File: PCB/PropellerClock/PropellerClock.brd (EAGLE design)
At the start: 100 x 50 mm, 32 parts

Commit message: 基板第一弾完成
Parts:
- removed IC2: (no value), v-reg:78XXL
- added C4: (no value), rcl:C2012
- U$2: value CR2032-HOLDER -> CR2032-HOLDER2; device CR2032-holder:CR2032-HOLDER -> CR2032-holder:CR2032-HOLDER2
- moved U$2 12.1 mm to (5.08, 13.3), flipped to the top, turned to 180 degrees
- moved IC1 5.85 mm to (12.1, 38.7)
- moved R1 2.54 mm to (21.0, 40.0)
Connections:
- removed net 3VR: IC1.8, U$2.3VR
- removed net N$1: C2.1, C3.1, IC2.IN, PAD2.1
- new net N$4: IC1.8, U$2.+3V
- net +3V3: now also C2.1, C3.1, C4.1, PAD2.1; no longer IC2.OUT
- net GND: now also C4.2; no longer IC2.GND
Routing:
- net +3V3: track 66.2 -> 91.9 mm
- net N$4: track 0.00 -> 18.4 mm
- net N$1: track 17.2 -> 0.00 mm
- net 3VR: track 15.6 -> 0.00 mm
- net N$8: track 28.7 -> 37.5 mm
- net N$5: track 40.9 -> 48.7 mm
- net GND: track 240.4 -> 235.6 mm
- removed copper zone on layer 16, net 3VR

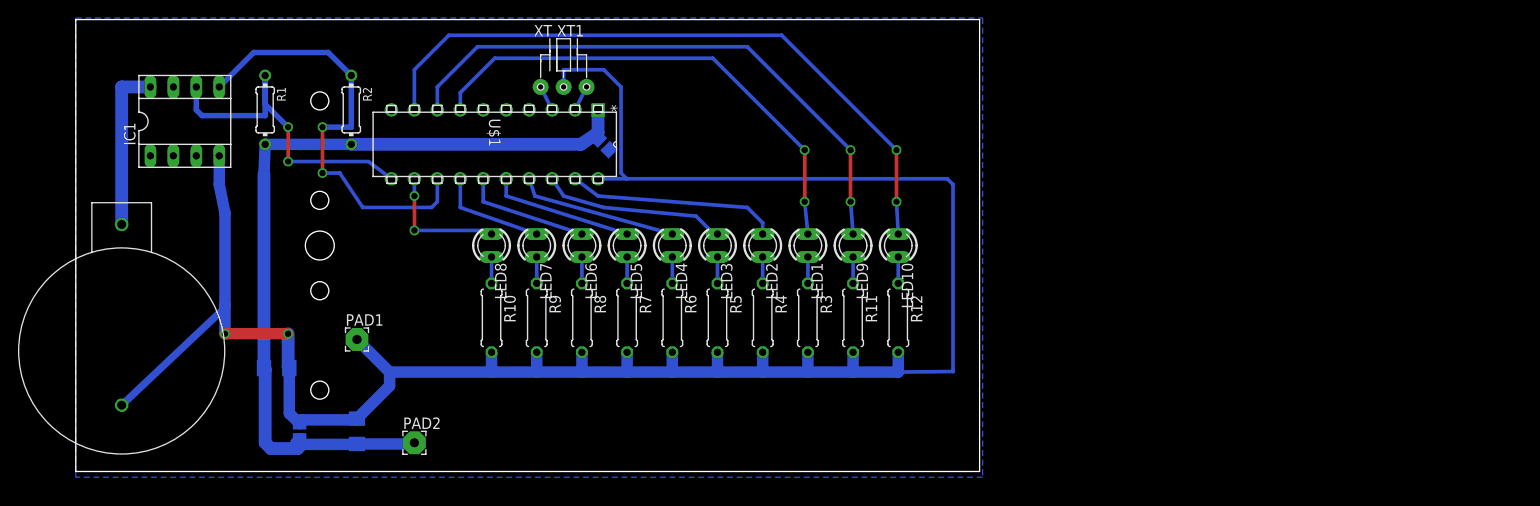
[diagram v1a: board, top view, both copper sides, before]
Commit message: プロペラ部の回路を作成
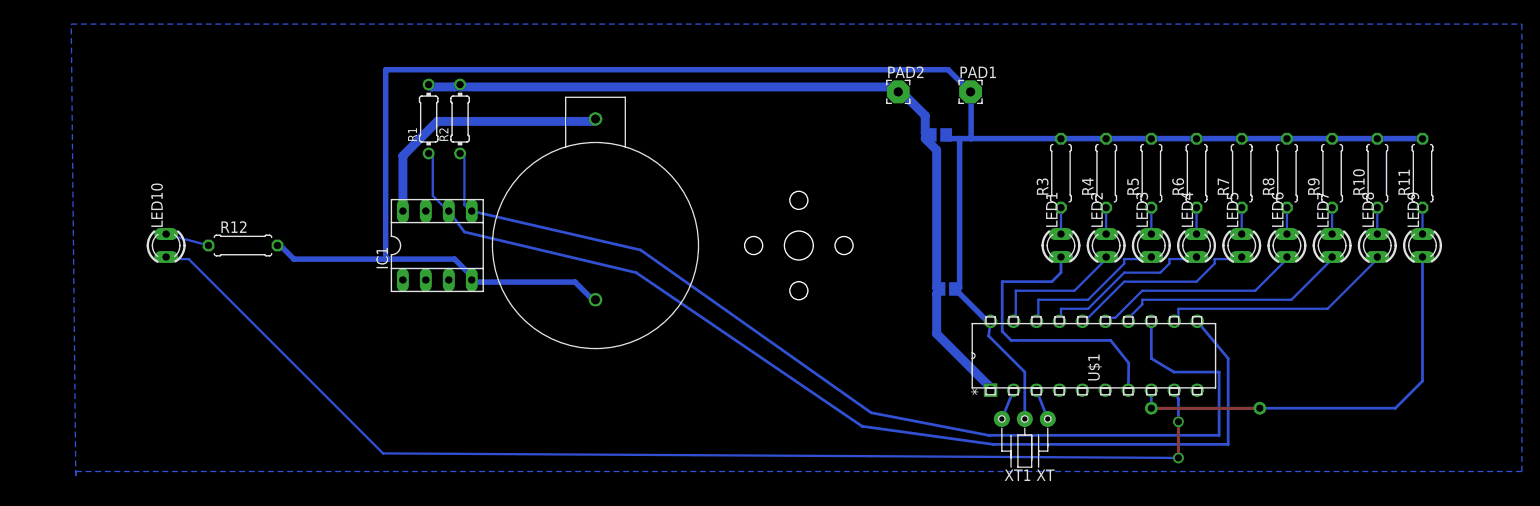
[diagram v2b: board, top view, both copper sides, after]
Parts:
- removed C1, C2: (no value), rcl:C3216
- moved R10 99.3 mm to (144.0, 33.0), turned to 90 degrees
- moved LED8 98.0 mm to (144.0, 25.0), turned to 90 degrees
- moved U$1 90.5 mm to (124.1, 16.6), turned to 90 degrees
- moved R9 89.4 mm to (139.0, 33.0), turned to 90 degrees
- moved LED7 88.0 mm to (139.0, 25.0), turned to 90 degrees
- moved LED10 81.0 mm to (10.0, 25.0), turned to 90 degrees
- moved R8 79.6 mm to (134.0, 33.0), turned to 90 degrees
- moved LED6 78.0 mm to (134.0, 25.0), turned to 90 degrees
- moved C3 77.9 mm to (95.4, 37.2), turned to 180 degrees
- moved PAD1 73.2 mm to (99.0, 42.0)
- moved R12 72.9 mm to (18.5, 25.0), turned to 0 degrees
- moved R7 69.9 mm to (129.0, 33.0), turned to 90 degrees
- moved LED5 68.0 mm to (129.0, 25.0), turned to 90 degrees
- moved XT1 67.6 mm to (105.0, 2.00), turned to 180 degrees
- moved PAD2 66.1 mm to (91.0, 42.0)
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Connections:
- net +3V3: no longer C1.1, C2.1
- net GND: no longer C1.2, C2.2
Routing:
- net N$8: track 37.5 -> 115.6 mm, vias 2 -> 0
- net N$5: track 48.7 -> 115.2 mm, vias 2 -> 0
- net LED_BUS10: track 73.9 -> 128.7 mm
- net LED_BUS1: track 55.1 -> 32.8 mm, vias 2 -> 0
- net GND: track 235.6 -> 217.8 mm, vias 2 -> 0
- net LED_BUS9: track 64.1 -> 47.0 mm
- net LED_BUS7: track 12.1 -> 26.1 mm
- net LED_BUS8: track 14.4 -> 26.1 mm, vias 2 -> 0
- net N$4: track 18.4 -> 29.1 mm
- net LED_BUS6: track 14.0 -> 23.3 mm
- net LED_BUS2: track 23.4 -> 15.1 mm
- net LED_BUS5: track 15.9 -> 21.1 mm
- net LED_BUS3: track 20.4 -> 17.3 mm
- net N$18: track 2.92 -> 4.86 mm
- net LED_BUS4: track 17.8 -> 19.2 mm
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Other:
- board outline removed
